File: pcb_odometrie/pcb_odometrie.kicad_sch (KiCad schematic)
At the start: 30 parts, among them J1 USB_C_Receptacle_USB2.0_16P, J2 Conn_ST_STDC14, J3 1755736, J4 Conn_02x05_Row_Letter_First, J5 Conn_02x04_Row_Letter_First, U1 STM32G491KEU6

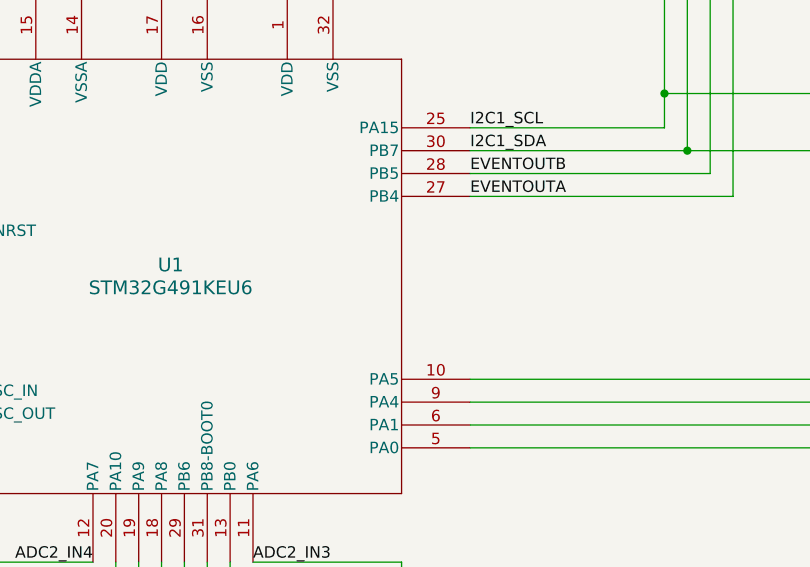
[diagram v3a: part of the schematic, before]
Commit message: changement pin encodeur pour avoir la fonction timer
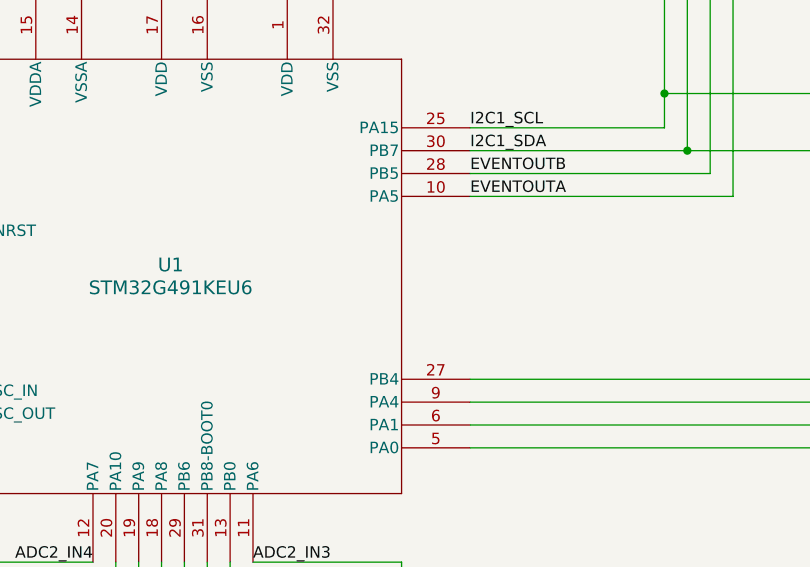
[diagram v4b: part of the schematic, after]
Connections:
- net EVENTOUTA: now also U1.10 (PA5); no longer U1.27 (PB4)
- net at J5.a3 (Pin_a3): now also U1.27 (PB4); no longer U1.10 (PA5)

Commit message: connecteur 14pin avec detrompage + renumerotation TOF
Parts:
- J2: footprint Connector_PinHeader_1.27mm:PinHeader_2x07_P1.27mm_Vertical -> Modelec:CONN14_3220-14_CNC
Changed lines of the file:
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@@
 			)
 		)
-		(property "Footprint" "Connector_PinHeader_1.27mm:PinHeader_2x07_P1.27mm_Vertical"
+		(property "Footprint" "Modelec:CONN14_3220-14_CNC"
 			(at 49.53 132.08 0)
 			(effects

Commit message: version finale PCB odometrie
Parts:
- removed J4: Conn_02x05_Row_Letter_First, Connector_PinSocket_1.27mm:PinSocket_2x05_P1.27mm_Vertical, symbol Connector_Generic:Conn_02x05_Row_Letter_First
- added J4: Conn_02x06_Row_Letter_First, Connector_PinSocket_2.54mm:PinSocket_2x06_P2.54mm_Vertical, symbol Connector_Generic:Conn_02x06_Row_Letter_First
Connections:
- net +12V: now also J4.a1 (Pin_a1), J4.b1 (Pin_b1)
- net CTA: now also J4.a6 (Pin_a6)
- net CTB: now also J4.b6 (Pin_b6)
- net ENA: now also J4.a5 (Pin_a5)
- net ENB: now also J4.b5 (Pin_b5)
- net GND: now also J4.a2 (Pin_a2), J4.b2 (Pin_b2)
- net IN1A: now also J4.a3 (Pin_a3)
- net IN1B: now also J4.b3 (Pin_b3)
- net IN2A: now also J4.a4 (Pin_a4)
- net IN2B: now also J4.b4 (Pin_b4)
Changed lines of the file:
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@@
 	(wire
 		(pts
+			(xy 140.97 173.99) (xy 144.78 173.99)
+		)
+		(stroke
+			(width 0)
+			(type default)
+		)
+	)
+	(wire
+		(pts
 			(xy 118.11 83.82) (xy 118.11 78.74)
 		)
@@
 	(wire
 		(pts
+			(xy 124.46 173.99) (xy 128.27 173.99)
+		)
+		(stroke
+			(width 0)
+			(type default)
+		)
+	)
+	(wire
+		(pts
 			(xy 77.47 127) (xy 62.23 127)
 		)
@@
 	(wire
 		(pts
-			(xy 144.78 173.99) (xy 140.97 173.99)
+			(xy 144.78 171.45) (xy 140.97 171.45)
 		)
 		(stroke
@@
 	(wire
 		(pts
-			(xy 124.46 173.99) (xy 128.27 173.99)
+			(xy 124.46 171.45) (xy 128.27 171.45)
 		)
 		(stroke
@@
 	)
 	(symbol
-		(lib_id "Connector_Generic:Conn_02x05_Row_Letter_First")
-		(at 133.35 179.07 0)
-		(unit 1)
-		(exclude_from_sim no)
-		(in_bom yes)
-		(on_board yes)
-		(dnp no)
-		(fields_autoplaced yes)
-		(property "Reference" "J4"
-			(at 134.62 167.64 0)
-			(effects
-				(font
-					(size 1.27 1.27)
-				)
-			)
-		)
-		(property "Value" "Conn_02x05_Row_Letter_First"
-			(at 134.62 170.18 0)
-			(effects
-				(font
-					(size 1.27 1.27)
-				)
-			)
-		)
-		(property "Footprint" "Connector_PinSocket_1.27mm:PinSocket_2x05_P1.27mm_Vertical"
-			(at 133.35 179.07 0)
-			(effects
-				(font
-					(size 1.27 1.27)
-				)
-				(hide yes)
-			)
-		)
-		(property "Datasheet" "~"
-			(at 133.35 179.07 0)
-			(effects
-				(font
-					(size 1.27 1.27)
-				)
-				(hide yes)
-			)
-		)
-		(property "Description" "Generic connector, double row, 02x05, row letter first pin numbering scheme (pin number consists of a letter for the row and a number for the pin index in this row. a1, ..., aN; b1, ..., bN), script generated (kicad-library-utils/schlib/autogen/connector/)"
-			(at 133.35 179.07 0)
-			(effects
-				(font
-					(size 1.27 1.27)
-				)
-				(hide yes)
-			)
-		)
-		(pin "a5"
-		)
-		(pin "a1"
-		)
-		(pin "a2"
-		)
-		(pin "a3"
-		)
-		(pin "a4"
-		)
-		(pin "b2"
-		)
-		(pin "b3"
-		)
-		(pin "b4"
-		)
-		(pin "b5"
-		)
-		(pin "b1"
-		)
-		(instances
-			(project ""
-				(path "/459e8b64-8c98-43d9-80d0-5d1e7550d13c"
-					(reference "J4")
-					(unit 1)
-				)
-			)
-		)
-	)
-	(symbol
 		(lib_id "power:+12V")
 		(at 241.3 130.81 0)
@@
 	(symbol
 		(lib_id "power:+12V")
-		(at 144.78 173.99 0)
+		(at 144.78 171.45 0)
 		(unit 1)
 		(exclude_from_sim no)
@@
 		(dnp no)
 		(property "Reference" "#PWR043"
-			(at 144.78 177.8 0)
+			(at 144.78 175.26 0)
 			(effects
 				(font
@@
 		)
 		(property "Value" "+12V"
-			(at 145.542 172.72 0)
+			(at 145.542 170.18 0)
 			(effects
 				(font
@@
 		)
 		(property "Footprint" ""
-			(at 144.78 173.99 0)
+			(at 144.78 171.45 0)
 			(effects
 				(font
@@
 		)
 		(property "Datasheet" ""
-			(at 144.78 173.99 0)
+			(at 144.78 171.45 0)
 			(effects
 				(font
@@
 		)
 		(property "Description" "Power symbol creates a global label with name \"+12V\""
-			(at 144.78 173.99 0)
+			(at 144.78 171.45 0)
 			(effects
 				(font
@@
 	)
 	(symbol
+		(lib_id "power:GND")
+		(at 144.78 173.99 90)
+		(unit 1)
+		(exclude_from_sim no)
+		(in_bom yes)
+		(on_board yes)
+		(dnp no)
+		(property "Reference" "#PWR055"
+			(at 151.13 173.99 0)
+			(effects
+				(font
+					(size 1.27 1.27)
+				)
+				(hide yes)
+			)
+		)
+		(property "Value" "GND"
+			(at 147.828 173.99 90)
+			(effects
+				(font
+					(size 1.27 1.27)
+				)
+				(justify right)
+			)
+		)
+		(property "Footprint" ""
+			(at 144.78 173.99 0)
+			(effects
+				(font
+					(size 1.27 1.27)
+				)
+				(hide yes)
+			)
+		)
+		(property "Datasheet" ""
+			(at 144.78 173.99 0)
+			(effects
+				(font
+					(size 1.27 1.27)
+				)
+				(hide yes)
+			)
+		)
+		(property "Description" "Power symbol creates a global label with name \"GND\" , ground"
+			(at 144.78 173.99 0)
+			(effects
+				(font
+					(size 1.27 1.27)
+				)
+				(hide yes)
+			)
+		)
+		(pin "1"
+		)
+		(instances
+			(project "pcb_odometrie"
+				(path "/459e8b64-8c98-43d9-80d0-5d1e7550d13c"
+					(reference "#PWR055")
+					(unit 1)
+				)
+			)
+		)
+	)
+	(symbol
 		(lib_id "power:+3V3")
 		(at 95.25 33.02 90)
@@
 	)
 	(symbol
+		(lib_id "power:GND")
+		(at 124.46 173.99 270)
+		(unit 1)
+		(exclude_from_sim no)
+		(in_bom yes)
+		(on_board yes)
+		(dnp no)
+		(property "Reference" "#PWR054"
+			(at 118.11 173.99 0)
+			(effects
+				(font
+					(size 1.27 1.27)
+				)
+				(hide yes)
+			)
+		)
+		(property "Value" "GND"
+			(at 121.666 173.99 90)
+			(effects
+				(font
+					(size 1.27 1.27)
+				)
+				(justify right)
+			)
+		)
+		(property "Footprint" ""
+			(at 124.46 173.99 0)
+			(effects
+				(font
+					(size 1.27 1.27)
+				)
+				(hide yes)
+			)
+		)
+		(property "Datasheet" ""
+			(at 124.46 173.99 0)
+			(effects
+				(font
+					(size 1.27 1.27)
+				)
+				(hide yes)
+			)
+		)
+		(property "Description" "Power symbol creates a global label with name \"GND\" , ground"
+			(at 124.46 173.99 0)
+			(effects
+				(font
+					(size 1.27 1.27)
+				)
+				(hide yes)
+			)
+		)
+		(pin "1"
+		)
+		(instances
+			(project "pcb_odometrie"
+				(path "/459e8b64-8c98-43d9-80d0-5d1e7550d13c"
+					(reference "#PWR054")
+					(unit 1)
+				)
+			)
+		)
+	)
+	(symbol
 		(lib_id "Connector_Generic:Conn_02x04_Row_Letter_First")
 		(at 231.14 133.35 0)
@@
 	(symbol
 		(lib_id "power:+12V")
-		(at 124.46 173.99 0)
+		(at 124.46 171.45 0)
 		(mirror y)
 		(unit 1)
@@
 		(dnp no)
 		(property "Reference" "#PWR044"
-			(at 124.46 177.8 0)
+			(at 124.46 175.26 0)
 			(effects
 				(font
@@
 		)
 		(property "Value" "+12V"
-			(at 122.682 172.974 0)
+			(at 122.682 170.434 0)
 			(effects
 				(font
@@
 		)
 		(property "Footprint" ""
-			(at 124.46 173.99 0)
+			(at 124.46 171.45 0)
 			(effects
 				(font
@@
 		)
 		(property "Datasheet" ""
-			(at 124.46 173.99 0)
+			(at 124.46 171.45 0)
 			(effects
 				(font
@@
 		)
 		(property "Description" "Power symbol creates a global label with name \"+12V\""
-			(at 124.46 173.99 0)
+			(at 124.46 171.45 0)
 			(effects
 				(font
@@
 					(unit 1)
 				)
+			)
+		)
+	)
+	(symbol
+		(lib_id "Connector_Generic:Conn_02x06_Row_Letter_First")
+		(at 133.35 176.53 0)
+		(unit 1)
+		(exclude_from_sim no)
+		(in_bom yes)
+		(on_board yes)
+		(dnp no)
+		(fields_autoplaced yes)
+		(property "Reference" "J4"
+			(at 134.62 165.1 0)
+			(effects
+				(font
+					(size 1.27 1.27)
+				)
+			)
+		)
+		(property "Value" "Conn_02x06_Row_Letter_First"
+			(at 134.62 167.64 0)
+			(effects
+				(font
+					(size 1.27 1.27)
+				)
+			)
+		)
+		(property "Footprint" "Connector_PinSocket_2.54mm:PinSocket_2x06_P2.54mm_Vertical"
+			(at 133.35 176.53 0)
+			(effects
+				(font
+					(size 1.27 1.27)
+				)
+				(hide yes)
+			)
+		)
+		(property "Datasheet" "~"
+			(at 133.35 176.53 0)
+			(effects
+				(font
+					(size 1.27 1.27)
+				)
+				(hide yes)
+			)
+		)
+		(property "Description" "Generic connector, double row, 02x06, row letter first pin numbering scheme (pin number consists of a letter for the row and a number for the pin index in this row. a1, ..., aN; b1, ..., bN), script generated (kicad-library-utils/schlib/autogen/connector/)"
+			(at 133.35 176.53 0)
+			(effects
+				(font
+					(size 1.27 1.27)
+				)
+				(hide yes)
+			)
+		)
+		(pin "b5"
+		)
+		(pin "a3"
+		)
+		(pin "a1"
+		)
+		(pin "b1"
+		)
+		(pin "b2"
+		)
+		(pin "b3"
+		)
+		(pin "a2"
+		)
+		(pin "a4"
+		)
+		(pin "b6"
+		)
+		(pin "a5"
+		)
+		(pin "a6"
+		)
+		(pin "b4"
+		)
+		(instances
+			(project ""
+				(path "/459e8b64-8c98-43d9-80d0-5d1e7550d13c"
+					(reference "J4")
+					(unit 1)
+				)

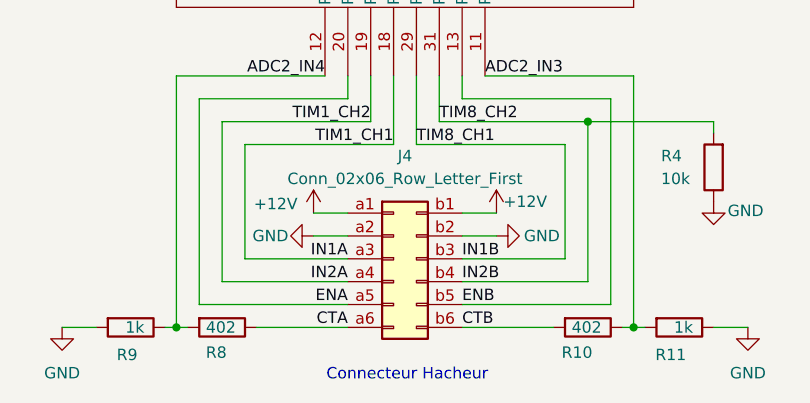
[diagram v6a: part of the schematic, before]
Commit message: Ajout BAU servo PAMI, finitions PCB Actionneurs, fichier fab stencil. Version commandée PAMI & Actionneurs
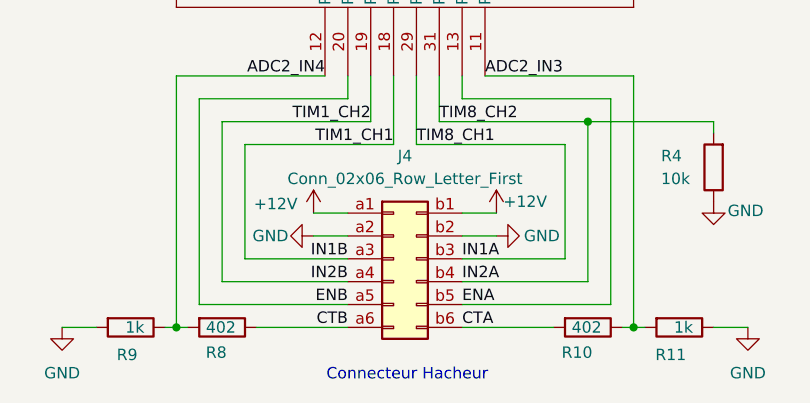
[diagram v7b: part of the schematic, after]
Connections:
- net CTA: now also J4.b6 (Pin_b6), R10.2; no longer J4.a6 (Pin_a6), R8.1
- net CTB: now also J4.a6 (Pin_a6), R8.1; no longer J4.b6 (Pin_b6), R10.2
- net ENA: now also J4.b5 (Pin_b5), U1.13 (PB0); no longer J4.a5 (Pin_a5), U1.20 (PA10)
- net ENB: now also J4.a5 (Pin_a5), U1.20 (PA10); no longer J4.b5 (Pin_b5), U1.13 (PB0)
- net IN1A: now also J4.b3 (Pin_b3), U1.29 (PB6); no longer J4.a3 (Pin_a3), U1.18 (PA8)
- net IN1B: now also J4.a3 (Pin_a3), U1.18 (PA8); no longer J4.b3 (Pin_b3), U1.29 (PB6)
- net IN2A: now also J4.b4 (Pin_b4), R4.2, U1.31 (PB8-BOOT0); no longer J4.a4 (Pin_a4), U1.19 (PA9)
- net IN2B: now also J4.a4 (Pin_a4), U1.19 (PA9); no longer J4.b4 (Pin_b4), R4.2, U1.31 (PB8-BOOT0)
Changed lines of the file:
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@@
 		)
 	)
-	(label "IN1A"
+	(label "IN1B"
 		(at 128.27 176.53 180)
 		(effects
@@
 		)
 	)
-	(label "IN2A"
+	(label "IN2B"
 		(at 128.27 179.07 180)
 		(effects
@@
 		)
 	)
-	(label "CTB"
+	(label "CTA"
 		(at 140.97 184.15 0)
 		(effects
@@
 		)
 	)
-	(label "ENA"
+	(label "ENB"
 		(at 128.27 181.61 180)
 		(effects
@@
 		)
 	)
-	(label "IN2B"
+	(label "IN2A"
 		(at 140.97 179.07 0)
 		(effects
@@
 		)
 	)
-	(label "CTA"
+	(label "CTB"
 		(at 128.27 184.15 180)
 		(effects
@@
 		)
 	)
-	(label "ENB"
+	(label "ENA"
 		(at 140.97 181.61 0)
 		(effects
@@
 		)
 	)
-	(label "IN1B"
+	(label "IN1A"
 		(at 140.97 176.53 0)
 		(effects
